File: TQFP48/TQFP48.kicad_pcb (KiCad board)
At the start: 2 copper layers, 61 x 17.8 mm, 9 parts, among them J1 Conn_01x24, J2 Conn_02x24_Counter_Clockwise, J3 Conn_02x24_Counter_Clockwise, J4 Conn_01x24, J5 Conn_01x05

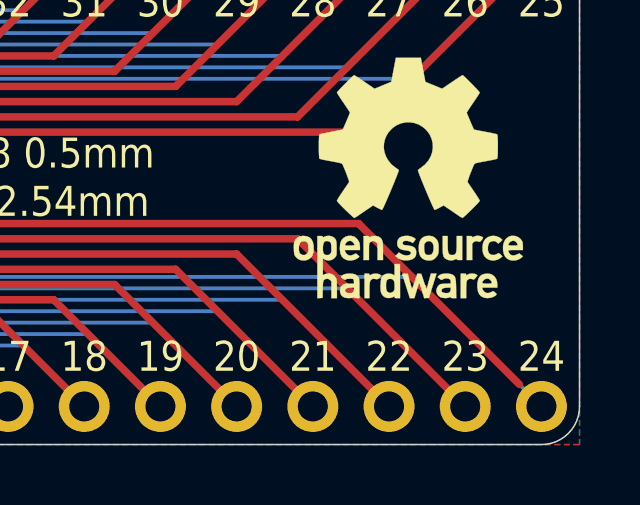
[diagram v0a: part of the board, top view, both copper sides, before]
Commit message: Fixed unconnected trace on TQFP48 breakout
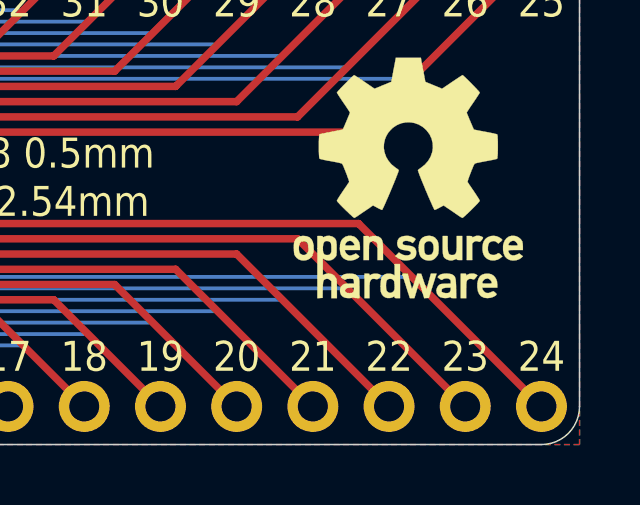
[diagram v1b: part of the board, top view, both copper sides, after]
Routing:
- net Net-(J1-Pad24): track 54.5 -> 55.6 mm
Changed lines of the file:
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@@
   (title_block
     (title "TQFP48 to DIP48 Breakout Board")
-    (date 2020-04-19)
-    (rev 2)
+    (date 2022-07-14)
+    (rev 3)
     (company SirBoard)
     (comment 1 "TQFP48 P =0.5mm")
@@
   (segment (start 72.324876 36.558788) (end 72.850088 37.084) (width 0.25) (layer F.Cu) (net 1))
   (segment (start 72.850088 37.084) (end 90.551 37.084) (width 0.25) (layer F.Cu) (net 1))
-  (segment (start 90.551 37.084) (end 95.911955 42.444955) (width 0.25) (layer F.Cu) (net 1))
   (segment (start 95.521152 42.054152) (end 96.647 43.18) (width 0.127) (layer B.Cu) (net 1))
   (segment (start 73.85027 38.862) (end 92.329 38.862) (width 0.127) (layer B.Cu) (net 1))
   (segment (start 92.329 38.862) (end 95.521152 42.054152) (width 0.127) (layer B.Cu) (net 1))
   (segment (start 71.069761 36.081491) (end 73.85027 38.862) (width 0.127) (layer B.Cu) (net 1))
+  (segment (start 90.551 37.084) (end 96.647 43.18) (width 0.25) (layer F.Cu) (net 1))
   (segment (start 94.107 43.18) (end 88.519 37.592) (width 0.25) (layer F.Cu) (net 2))
   (segment (start 72.65098 37.592) (end 71.971322 36.912342) (width 0.25) (layer F.Cu) (net 2))
